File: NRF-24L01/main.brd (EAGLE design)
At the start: 160 x 100 mm, 17 parts

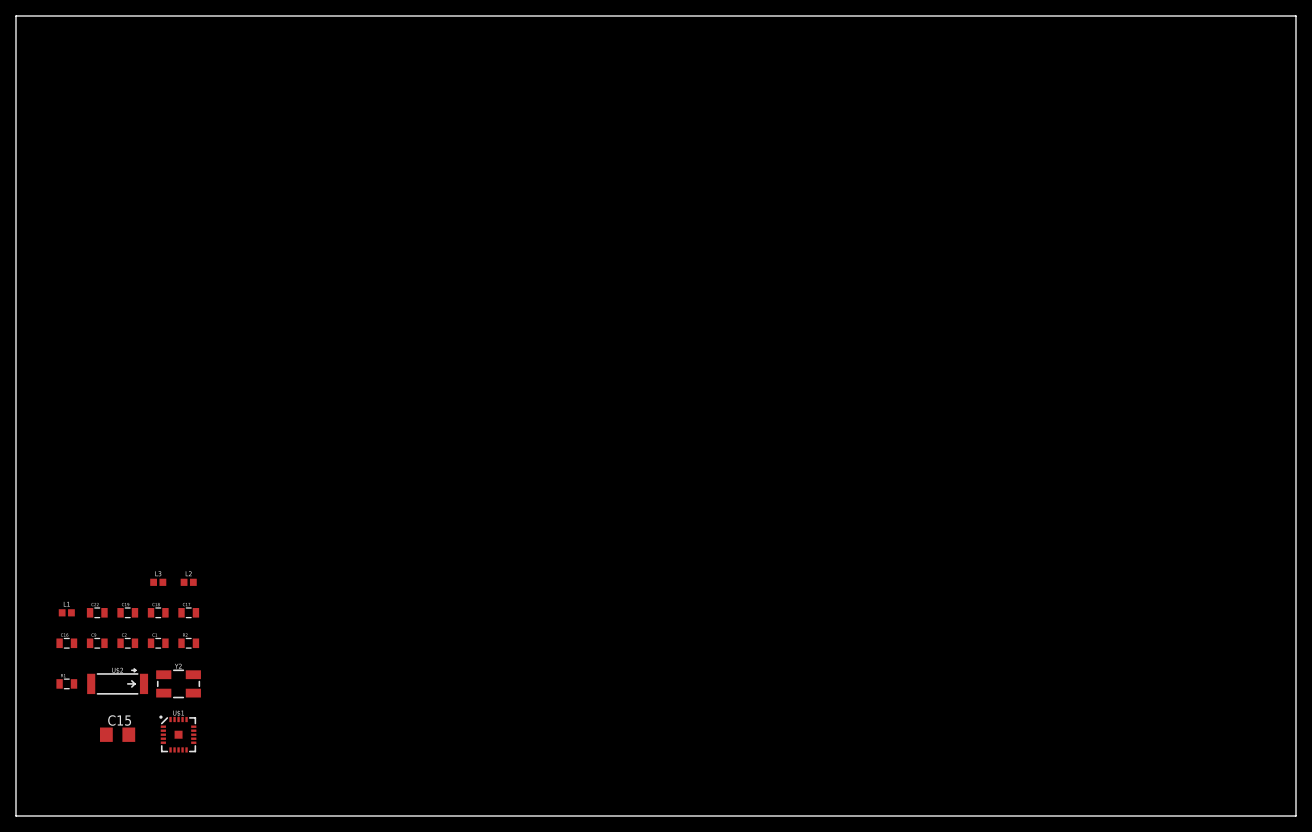
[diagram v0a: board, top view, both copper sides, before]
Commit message: add license
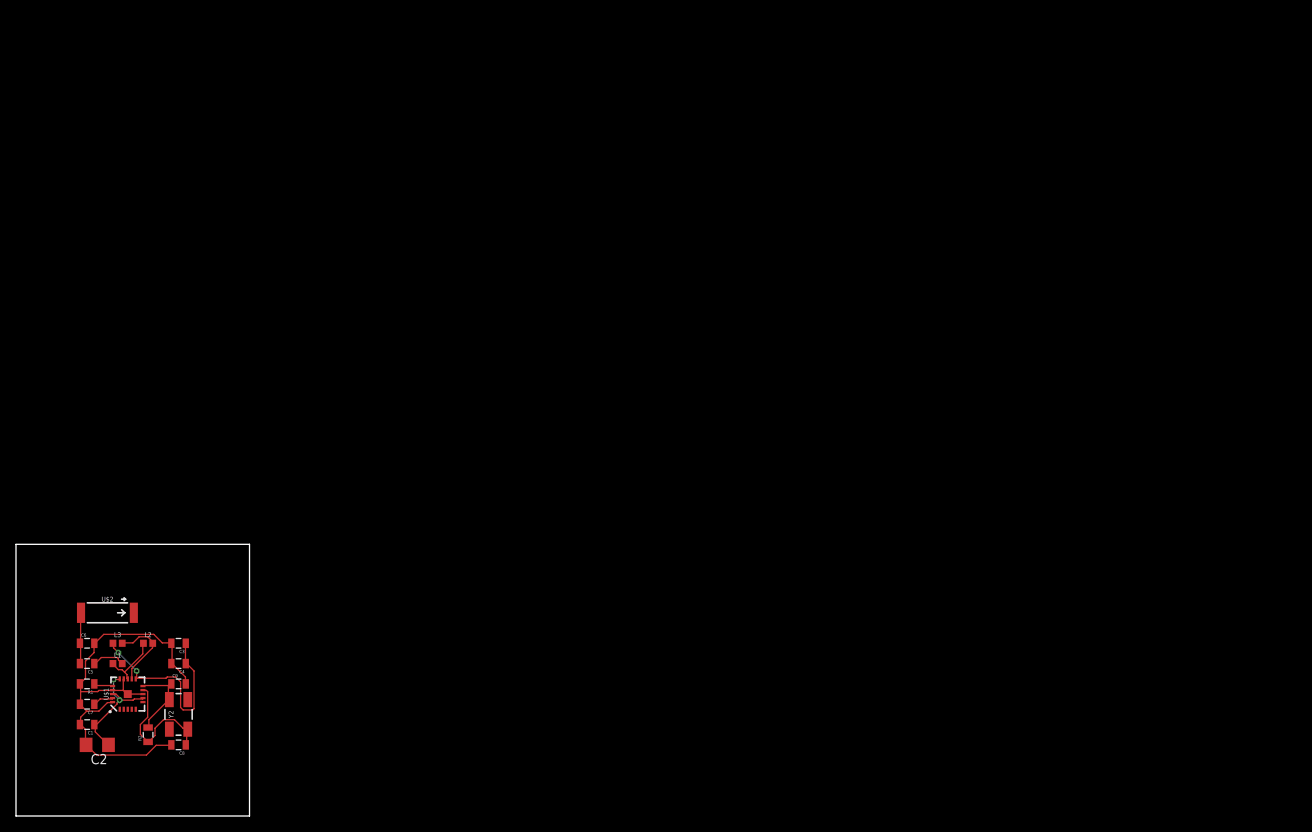
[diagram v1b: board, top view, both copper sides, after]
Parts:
- removed C15: 10uF, adafruit:C1206
- removed C16: 4.7p, SparkFun-Passives:0805
- removed C17: 1.5p, SparkFun-Passives:0805
- removed C18: 10p, SparkFun-Passives:0805
- removed C19: 1nF, SparkFun-Passives:0805
- removed C22: 1uF, SparkFun-Passives:0805
- added C3: 2.2nF, SparkFun-Passives:0805
- added C4: 4.7p, SparkFun-Passives:0805
- added C5: 1.5p, SparkFun-Passives:0805
- added C6: 10p, SparkFun-Passives:0805
- added C7: 1uF, SparkFun-Passives:0805
- added C8: 22p, SparkFun-Passives:0805
- C1: value 22p -> 1nF
- C2: value 22p -> 10uF; device SparkFun-Passives:0805 -> adafruit:C1206
- C9: value 2.2nF -> 22p
- moved C1 13.5 mm to (8.89, 11.4), turned to 180 degrees
- moved C2 13.3 mm to (10.2, 8.89), turned to 180 degrees
- moved R2 12.5 mm to (16.5, 10.2), turned to 90 degrees
- moved C9 11.4 mm to (20.3, 16.5)
- moved L3 9.16 mm to (12.7, 21.6)
- moved L2 9.16 mm to (16.5, 21.6)
- moved L1 8.98 mm to (12.7, 19.1)
- moved U$2 8.98 mm to (11.4, 25.4)
- moved U$1 8.13 mm to (14.0, 15.2), turned to 90 degrees
- moved Y2 3.81 mm to (20.3, 12.7), turned to 90 degrees
- moved R1 2.54 mm to (8.89, 16.5), turned to 180 degrees
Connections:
- net 3.3V: now also C1.1, C2.1; no longer C15.1, C19.1
- net GND: now also C3.2, C4.2, C6.2, C7.2, C8.2; no longer C15.2, C16.2, C18.2, C19.2, C22.2
- net N$16: now also C3.1, C4.1; no longer C16.1, C9.1
- net N$17: now also C7.1; no longer C22.1
- net N$19: now also C5.2, C6.1; no longer C17.2, C18.1
- net N$20: now also C8.1; no longer C1.1
- net N$21: now also C9.1; no longer C2.1
- net N$4: now also C5.1; no longer C17.1
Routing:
- net GND: track 0.00 -> 56.0 mm
- net N$16: track 0.00 -> 25.3 mm, vias 0 -> 2
- net N$20: track 0.00 -> 17.0 mm
- net 3.3V: track 0.00 -> 16.2 mm, vias 0 -> 2
- net N$21: track 0.00 -> 10.5 mm
- net N$15: track 0.00 -> 10.2 mm
- net N$14: track 0.00 -> 7.65 mm
- net N$19: track 0.00 -> 6.53 mm
- net N$4: track 0.00 -> 4.21 mm
- net N$17: track 0.00 -> 2.63 mm
- net N$18: track 0.00 -> 2.40 mm
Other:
- board size 160 x 100 mm -> 29.2 x 34 mm

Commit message: update
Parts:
- moved C9 6.35 mm to (15.2, 12.7)
- moved R1 6.35 mm to (3.81, 12.7)
- moved R2 6.35 mm to (11.4, 6.35)
- moved L1 6.35 mm to (7.62, 15.2)
- moved C1 6.35 mm to (3.81, 7.62)
- moved C2 6.35 mm to (5.08, 5.08)
- moved C4 6.35 mm to (15.2, 15.2)
- moved C5 6.35 mm to (3.81, 15.2)
- moved C7 6.35 mm to (3.81, 10.2)
- moved C8 6.35 mm to (15.2, 5.08)
- moved L2 6.35 mm to (11.4, 17.8)
- moved U$1 6.35 mm to (8.89, 11.4)
- moved C3 6.35 mm to (15.2, 17.8)
- moved C6 6.35 mm to (3.81, 17.8)
- moved L3 6.35 mm to (7.62, 17.8)
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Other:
- board size 29.2 x 34 mm -> 19 x 25.1 mm
